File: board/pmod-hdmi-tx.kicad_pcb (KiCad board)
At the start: 2 copper layers, 37.3 x 43.2 mm, 53 parts, among them P1 PMOD-CONN_6X2, U31 XC9140, U32 REG710-DBV

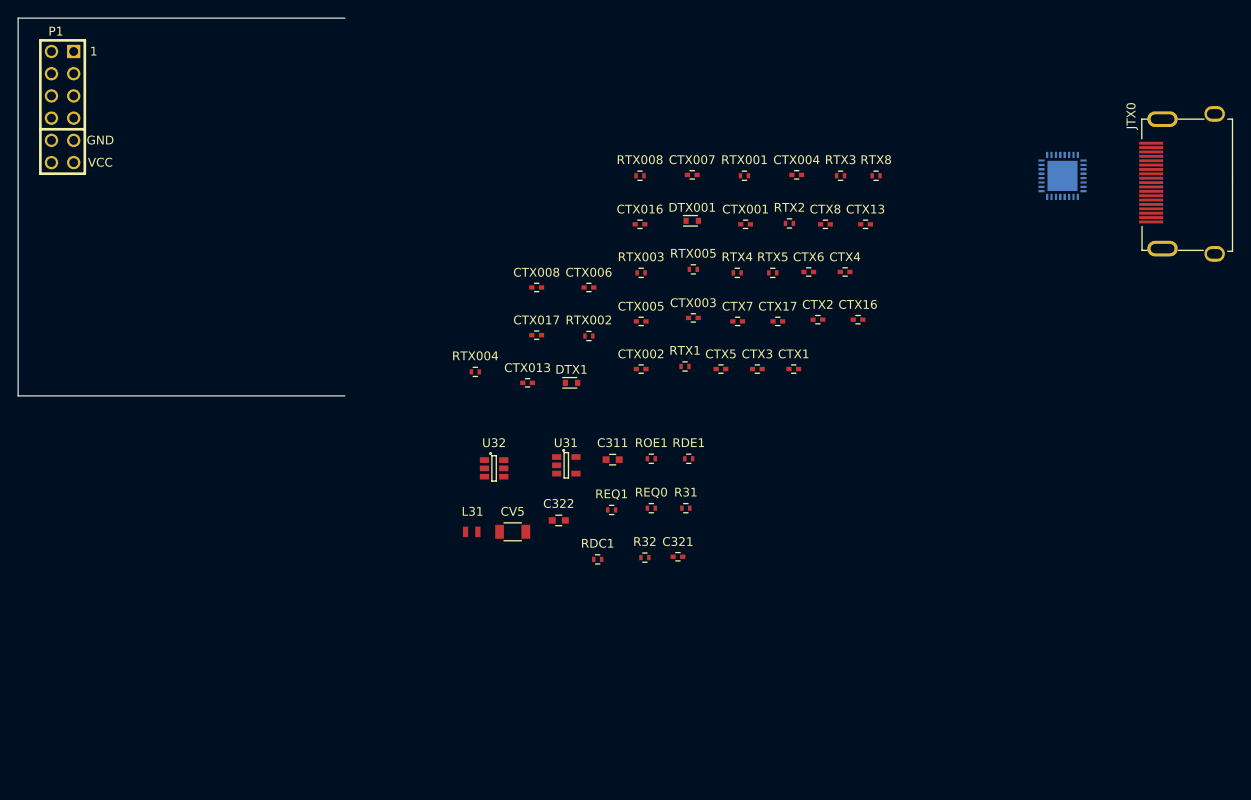
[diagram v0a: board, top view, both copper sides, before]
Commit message: Updating the PCB a little.
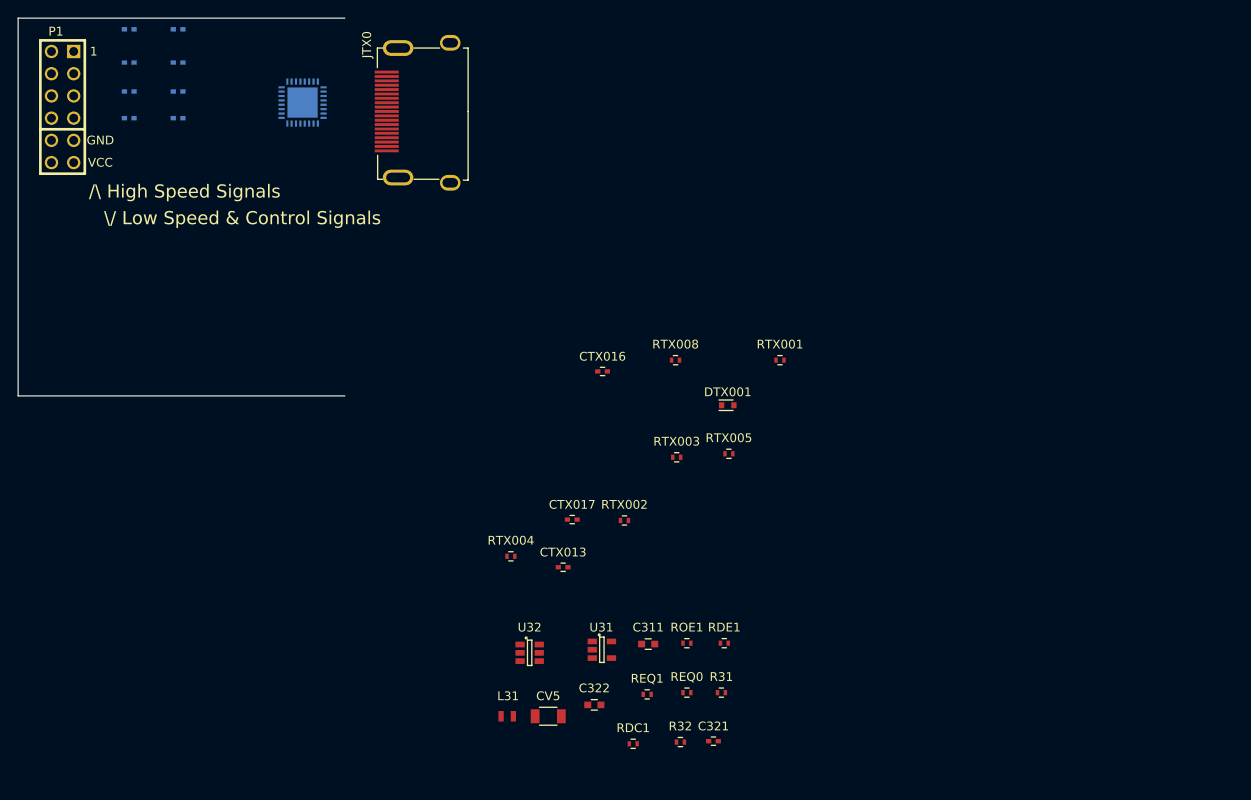
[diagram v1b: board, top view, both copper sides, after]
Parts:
- removed CTX1, CTX16, CTX17, CTX2, CTX3, CTX4, CTX5, CTX6, CTX7, CTX8: 100n, Capacitors_SMD:C_0402
- removed CTX13: 10n, Capacitors_SMD:C_0402
- removed DTX1: D, Diodes_SMD:SOD-523
- removed RTX1, RTX2, RTX4, RTX5: 2k2, Resistors_SMD:R_0402
- removed RTX3: 12k4, Resistors_SMD:R_0402
- removed RTX8: 27K, Resistors_SMD:R_0402
- CTX001, CTX002, CTX003, CTX004, CTX005, CTX006, CTX007, CTX008: value 100n -> 0.1uF; moved to B.Cu
- CTX016, CTX017: value 100n -> 0.1uF
- moved JTX0 87.8 mm to (68.8, 36.8)
- moved UTX0 87.3 mm to (57.9, 35.8)
- moved CTX004 76.9 mm to (38.1, 34.5), turned to 180 degrees
- moved CTX001 66.0 mm to (43.7, 37.6), turned to 180 degrees
- moved CTX002 65.2 mm to (38.1, 37.6), turned to 180 degrees
- moved CTX003 64.3 mm to (43.7, 34.5), turned to 180 degrees
- moved CTX007 61.1 mm to (43.7, 27.4), turned to 180 degrees
- moved CTX005 60.6 mm to (43.7, 31.2), turned to 180 degrees
- moved CTX006 58.5 mm to (38.1, 31.2), turned to 180 degrees
- moved CTX008 55.1 mm to (38.1, 27.4), turned to 180 degrees
- moved C311 21.5 mm to (97.4, 97.7)
- moved C322 21.5 mm to (91.3, 104.7)
- moved CTX013 21.5 mm to (87.7, 88.9)
- moved CV5 21.5 mm to (86.0, 106.0)
- moved DTX001 21.5 mm to (106.5, 70.4)
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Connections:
- P1 pad 3: /HDMI_TX0_EQ0 -> /HDMI_TX0_EQ1
- P1 pad 9: /HDMI_TX0_EQ1 -> /HDMI_TX0_EQ0
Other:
- board text added: "/\ High Speed Signals"
- board text added: "\/ Low Speed & Control Signals"

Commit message: First version from Phyllis.
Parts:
- ROE1, RTX004, RTX005: moved to B.Cu
- moved CTX008 74.5 mm to (93.5, 77.2)
- moved CTX006 73.5 mm to (93.5, 79.5)
- moved CTX004 72.8 mm to (93.5, 81.8)
- moved CTX002 72.3 mm to (93.5, 84.0)
- moved P1 70.4 mm to (85.5, 80.3)
- moved CTX007 69.7 mm to (93.5, 76.2)
- moved CTX005 68.7 mm to (93.5, 78.5)
- moved CTX003 68.0 mm to (93.5, 80.8)
- moved CTX001 67.4 mm to (93.5, 83.0)
- moved JTX0 65.1 mm to (114.4, 83.3)
- moved UTX0 63.7 mm to (101.5, 82.3)
- moved U32 32.5 mm to (116.2, 96.0)
- moved CV5 29.1 mm to (113.3, 95.7), turned to 270 degrees
- moved L31 28.0 mm to (107.6, 96.4), turned to 90 degrees
- moved C322 27.5 mm to (118.0, 98.3)
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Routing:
- net GND: track 0.00 -> 116.0 mm, vias 0 -> 32
- net VCC3V3: track 0.00 -> 109.5 mm, vias 0 -> 13
- net /HDMI_TX0_EQ0: track 0.00 -> 47.7 mm, vias 0 -> 2
- net /HDMI_TX0_SDA: track 0.00 -> 41.5 mm, vias 0 -> 2
- net /HDMI_TX0_DDET: track 0.00 -> 40.0 mm, vias 0 -> 2
- net /HDMI_TX0_CEC: track 0.00 -> 39.2 mm, vias 0 -> 2
- net /HDMI_TX0_SCL: track 0.00 -> 37.9 mm, vias 0 -> 2
- net /HDMI_TX0_EQ1: track 0.00 -> 37.2 mm, vias 0 -> 2
- net /HDMI_TX0_HPD: track 0.00 -> 36.5 mm, vias 0 -> 2
- net /HDMI_TX0_DCC_EN: track 0.00 -> 36.0 mm, vias 0 -> 2
- net TX05V0: track 0.00 -> 18.6 mm, vias 0 -> 1
- net /HDMI TX/HDMIP_TX0_HPD: track 0.00 -> 14.9 mm, vias 0 -> 2
- net /HDMI TX/HDMIP_TX0_SDA: track 0.00 -> 13.3 mm, vias 0 -> 1
- net /HDMI TX/HDMIP_TX0_SCL: track 0.00 -> 12.6 mm, vias 0 -> 1
- net /HDMI_TX0_D2-: track 0.00 -> 10.7 mm
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- added copper zone on B.Cu, net GND
- added copper zone on F.Cu, net GND
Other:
- board size 37.3 x 43.2 mm -> 42 x 43.3 mm
- net class Default: clearance 0.2 -> 0.127; trace_width 0.25 -> 0.127; via_dia 0.6 -> 0.5; via_drill 0.4 -> 0.25
- net class PWR added: clearance 0.127, trace_width 0.25, via_dia 0.5, via_drill 0.25
- rule trace_clearance: 0.2 -> 0.127
- rule trace_min: 0.2 -> 0.127
- rule via_min_drill: 0.3 -> 0
- rule via_min_size: 0.4 -> 0.5
- board text added: "& Control"
- board text added: "101.4"
- board text added: "104.5"
- board text added: "113.342"
- board text added: "122.4"
- board text added: "2.842"
- board text added: "21.0"
- board text added: "31.496"
- board text added: "42.0"
- board text added: "43.18"
- board text added: "70.162"
- board text added: "73.004"
- board text added: "76.0"
- board text added: "80.4"
- board text added: "91.0"
- board text added: "MTG HOLES ARE JUST CIRCLES"
- board text added: "Signals"
- board text added: "TEMPORARY FAB INFO ON ECO1"
- board text added: "UNTIL REAL FOOTPRINTS ARE ADDED"
- board text added: "\/ Low Speed"
- board text removed: "\/ Low Speed & Control Signals"

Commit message: Second version from Phyllis.
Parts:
- moved C321 1.40 mm to (120.0, 96.0)
- moved U32 1.40 mm to (117.6, 96.0)
- moved C322 1.40 mm to (119.4, 98.3)
- moved CV5 1.40 mm to (114.7, 95.7)
- moved R32 1.40 mm to (116.3, 98.3)
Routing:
- net GND: track 116.0 -> 436.1 mm, vias 32 -> 112
- net VCC3V3: track 109.5 -> 131.4 mm
- net TX05V0: track 18.6 -> 22.1 mm
- net (no net): vias 1 -> 0
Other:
- board text added: "1 OZ CU ALL LAYERS, WHEN FINISHED."
- board text added: "1. MATERIAL: FR408 1.6 mm THK, 4 LAYERS, EQUALLY SPACED,"
- board text added: "2. PLATED HOLES TO HAVE 1/2 OZ CU MIN."
- board text added: "3. PURPLE SOLDERMASK OVER BARE CU, BOTH SIDES."
- board text added: "4. ENIG (ELECTROLESS NICKEL IMMERSION GOLD)"
- board text added: "5. PERMANENTLY MARK DATE CODE AND"
- board text added: "CEC"
- board text added: "CLK+"
- board text added: "CLK-"
- board text added: "D0+"
- board text added: "D0-"
- board text added: "D1+"
- board text added: "D1-"
- board text added: "D2-"
- board text added: "D3-"
- board text added: "DCCE"
- board text added: "DCC_EN"
- board text added: "DDET"
- board text added: "EQ0"
- board text added: "EQ1"
- board text added: "GND"
- board text added: "HPD"
- board text added: "High Speed"
- board text added: "Low Speed & Control Signals"
- board text added: "MANUFACTURING SYMBOL ON BOTTOM."
- board text added: "NOTES: (UNLESS OTHERWISE SPECIFIED)"
- board text added: "SDA"
- board text added: "TOP"
- board text added: "VCC"
- board text removed: "& Control"
- board text removed: "/\ High Speed Signals"
- board text removed: "MTG HOLES ARE JUST CIRCLES"
- board text removed: "Signals"
- board text removed: "TEMPORARY FAB INFO ON ECO1"
- board text removed: "UNTIL REAL FOOTPRINTS ARE ADDED"
- board text removed: "\/ Low Speed"

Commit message: Update from templates + s/HPD/HOT/ + s/HPA/HOT/
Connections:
- net /HDMI TX/HDMIP_TX0_HPD renamed /HDMI TX/HDMIP_TX0_HOT
- net /HDMI_TX0_HPD renamed /HDMI_TX0_HOT
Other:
- board text added: "HOT"
- board text removed: "HPD"
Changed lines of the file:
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@@
   (net 11 /HDMI_TX0_D2+)
   (net 12 /HDMI_TX0_D2-)
-  (net 13 "/HDMI TX/HDMIP_TX0_HPD")
+  (net 13 "/HDMI TX/HDMIP_TX0_HOT")
   (net 14 TX05V0)
   (net 15 /HDMI_TX0_CEC)
@@
   (net 27 "Net-(L31-Pad2)")
   (net 28 /HDMI_TX0_SCL)
-  (net 29 /HDMI_TX0_HPD)
+  (net 29 /HDMI_TX0_HOT)
   (net 30 /HDMI_TX0_SDA)
   (net 31 /HDMI_TX0_EQ0)
@@
     (add_net "/HDMI TX/HDMIP_TX0_D2+")
     (add_net "/HDMI TX/HDMIP_TX0_D2-")
-    (add_net "/HDMI TX/HDMIP_TX0_HPD")
+    (add_net "/HDMI TX/HDMIP_TX0_HOT")
     (add_net "/HDMI TX/HDMIP_TX0_SCL")
     (add_net "/HDMI TX/HDMIP_TX0_SDA")
@@
     (add_net /HDMI_TX0_EQ0)
     (add_net /HDMI_TX0_EQ1)
-    (add_net /HDMI_TX0_HPD)
+    (add_net /HDMI_TX0_HOT)
     (add_net /HDMI_TX0_SCL)
     (add_net /HDMI_TX0_SDA)
@@
       (net 14 TX05V0))
     (pad 19 smd rect (at -4.5 -1.3 90) (size 0.3302 2.75) (layers F.Cu F.Paste F.Mask)
-      (net 13 "/HDMI TX/HDMIP_TX0_HPD"))
+      (net 13 "/HDMI TX/HDMIP_TX0_HOT"))
     (pad 0 thru_hole oval (at -7.55 0 90) (size 1.8 3.5) (drill oval 1.1 2.75) (layers *.Cu *.Mask F.SilkS))
     (pad 0 thru_hole oval (at 7.25 0 90) (size 1.8 3.5) (drill oval 1.1 2.75) (layers *.Cu *.Mask F.SilkS))
@@
       (net 47 "Net-(RTX003-Pad1)"))
     (pad 5 smd rect (at -2.4 -0.25 270) (size 0.7 0.25) (layers B.Cu B.Paste B.Mask)
-      (net 29 /HDMI_TX0_HPD))
+      (net 29 /HDMI_TX0_HOT))
     (pad 6 smd rect (at -2.4 -0.75 270) (size 0.7 0.25) (layers B.Cu B.Paste B.Mask)
       (net 30 /HDMI_TX0_SDA))
@@
       (net 26 "/HDMI TX/HDMIP_TX0_SDA"))
     (pad 21 smd rect (at 2.4 0.25 270) (size 0.7 0.25) (layers B.Cu B.Paste B.Mask)
-      (net 13 "/HDMI TX/HDMIP_TX0_HPD"))
+      (net 13 "/HDMI TX/HDMIP_TX0_HOT"))
     (pad 22 smd rect (at 2.4 0.75 270) (size 0.7 0.25) (layers B.Cu B.Paste B.Mask)
       (net 34 /HDMI_TX0_DCC_EN))
@@
       (net 2 GND))
     (pad 2 smd rect (at 0.55 0 270) (size 0.6 0.5) (layers F.Cu F.Paste F.Mask)
-      (net 13 "/HDMI TX/HDMIP_TX0_HPD"))
+      (net 13 "/HDMI TX/HDMIP_TX0_HOT"))
     (model Capacitors_SMD.3dshapes/C_0402.wrl
       (at (xyz 0 0 0))
@@
       (net 15 /HDMI_TX0_CEC))
     (pad 2 thru_hole circle (at 1.27 -3.81 270) (size 1.524 1.524) (drill 1.016) (layers *.Cu *.Mask F.SilkS)
-      (net 29 /HDMI_TX0_HPD))
+      (net 29 /HDMI_TX0_HOT))
     (pad 8 thru_hole circle (at -1.27 -3.81 270) (size 1.524 1.524) (drill 1.016) (layers *.Cu *.Mask F.SilkS)
       (net 30 /HDMI_TX0_SDA))
@@
     (effects (font (size 1 1) (thickness 0.15)) (justify mirror))
   )
-  (gr_text HPD (at 90.043 99.568) (layer B.SilkS)
+  (gr_text HOT (at 90.043 99.568) (layer B.SilkS)
     (effects (font (size 1 1) (thickness 0.15)) (justify mirror))
   )
@@
     (effects (font (size 1 1) (thickness 0.15)))
   )
-  (gr_text HPD (at 89.789 99.441) (layer F.SilkS)
+  (gr_text HOT (at 89.789 99.441) (layer F.SilkS)
     (effects (font (size 1 1) (thickness 0.15)))
   )

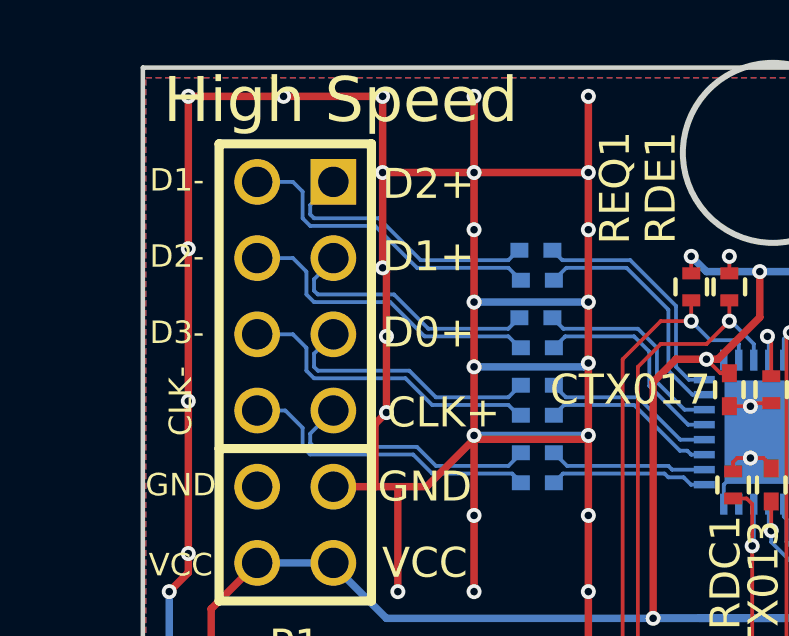
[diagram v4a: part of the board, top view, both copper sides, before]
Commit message: Reorganising the high speed signals.
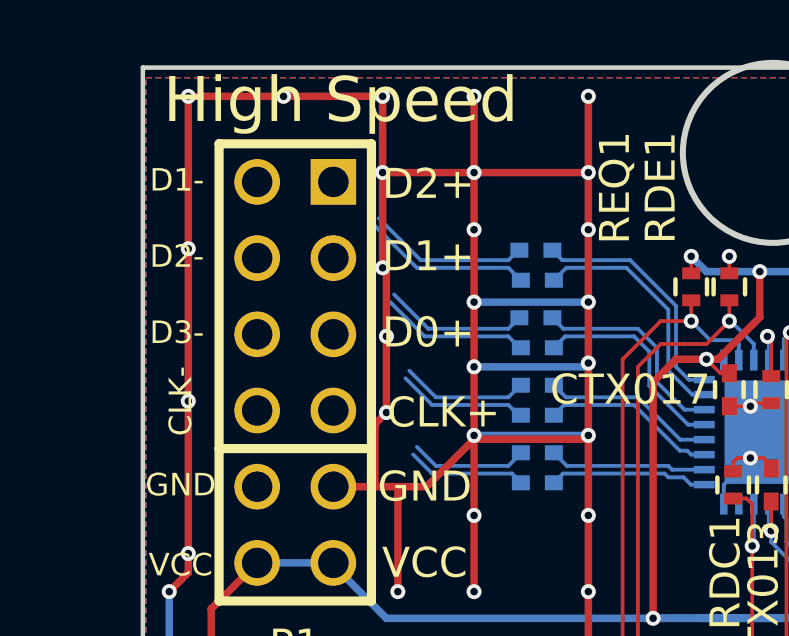
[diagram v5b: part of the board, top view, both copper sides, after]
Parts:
- P1: value PMOD-CONN_6X2 -> PMOD-Device-x2-Type-XHS-Alt
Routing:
- net /HDMI_TX0_CLK-: track 10.2 -> 3.99 mm
- net /HDMI_TX0_D0-: track 10.4 -> 4.36 mm
- net /HDMI_TX0_D1-: track 10.5 -> 4.98 mm
- net /HDMI_TX0_D2-: track 10.7 -> 5.61 mm
- net /HDMI_TX0_CLK+: track 8.94 -> 3.92 mm
- net /HDMI_TX0_D0+: track 8.83 -> 4.25 mm
- net /HDMI_TX0_D1+: track 8.87 -> 4.80 mm
- net /HDMI_TX0_D2+: track 9.14 -> 5.40 mm
